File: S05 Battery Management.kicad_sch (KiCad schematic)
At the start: 17 parts, among them Q10 DMT4011LFG, Q11 DMT4011LFG, Q12 DMP3018SFV, Q13 DMP3018SFV, Q14 DMP3018SFV, Q15 DMP3018SFV, Q8 DMT4011LFG, Q9 DMT4011LFG, U1 LTC1960

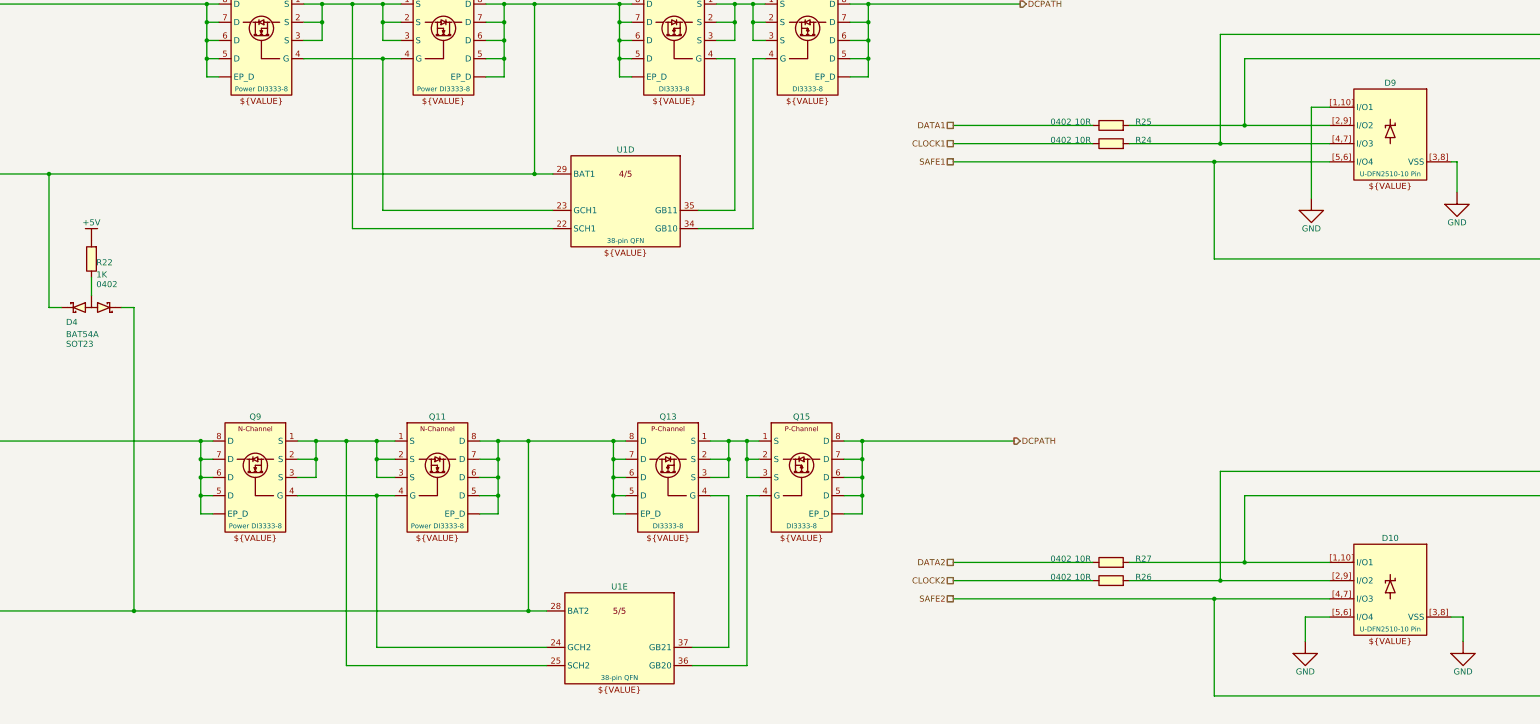
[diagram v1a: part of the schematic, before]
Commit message: Final-revision value changes and standard R/C symbols
Values (schematic and PCB):
- C2 100uF -> 82uF, matching the ordered 35SVPF82M
- C46, C47, C51 (TPS22811 DVDT) 4.7nF -> 1.8nF CC0402KRX7R9BB182 for a
  shorter output ramp
- R24-R27 10R -> 0R; D9, D10 and R36 DNP
- R14 0.01R -> 0.012R PA2512FKF7W0R012E

Symbols:
- All 160 resistors and capacitors now use Device:R, Device:C and
  Device:C_Polarized; the 76 per-value R/C symbols are removed from the
  project library. Connectivity is unchanged (netlist compared).
- Value is now the displayed field instead of ALTIUM_VALUE, which had left
  R1, C39 and R54 showing their old values. ALTIUM_VALUE synced with Value
  on R1, C39, R54, D1, Q1, Q3 and L1.
- Net-(C40-+) is now Net-(U5-ISNSP); renamed on the PCB and in the
  PWR 15A net class pattern.

Co-Authored-By: Claude Opus 5.5 <noreply@anthropic.com>
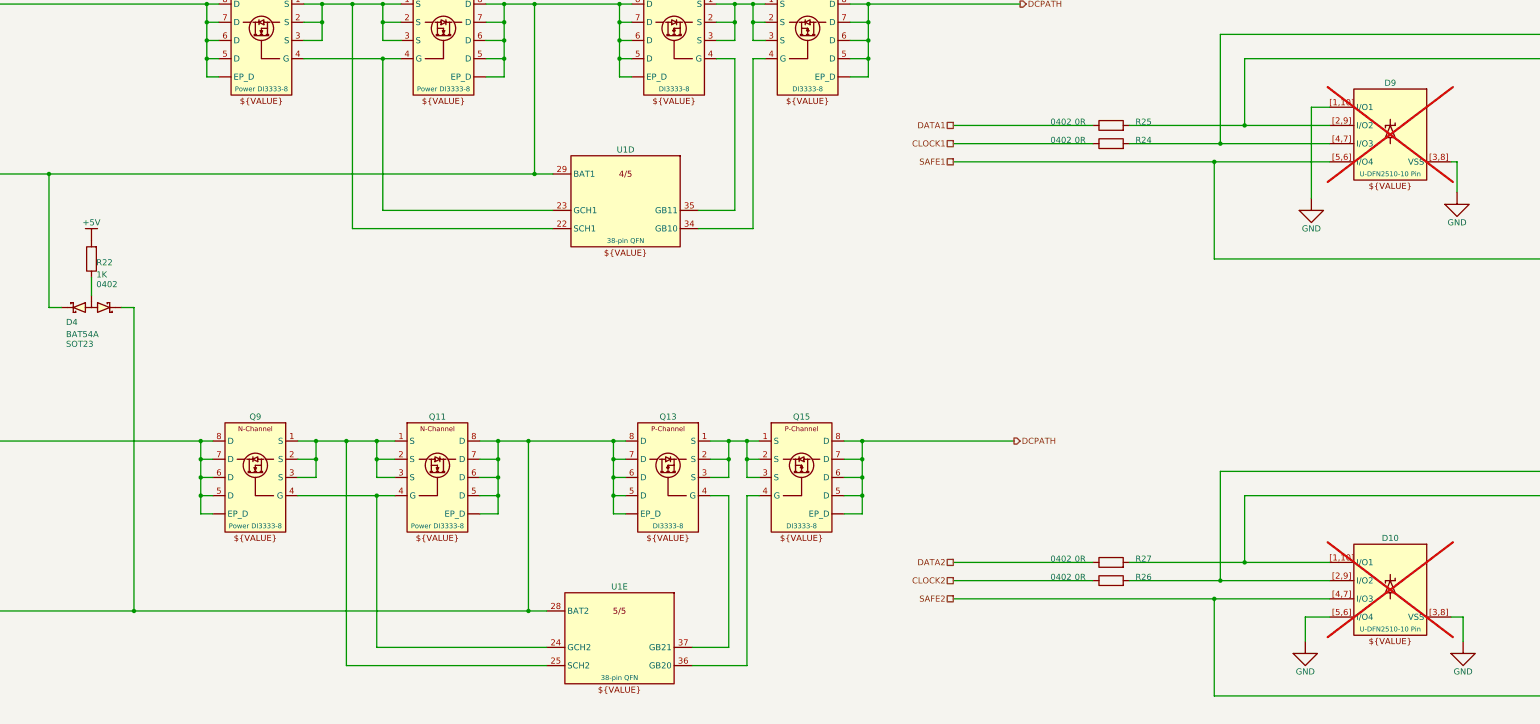
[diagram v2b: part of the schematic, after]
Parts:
- D10, D9: now not fitted
- R22: symbol Lattech Systems:Resistor 1K 1% 0402 -> Device:R
- R24, R25, R26, R27: value 10R -> 0R; symbol Lattech Systems:Resistor 10R 1% 0402 -> Device:R; ALTIUM_VALUE 10R -> 0R

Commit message: Retune load-switch OVLO and PG dividers; add design constraint notes
- R90-R92 1M -> 1.07M: OVLO trips at 14.0 V (13.40-14.69 V) and recovers
  below 12.75 V (at least 12.23 V), so a tripped switch always comes back
  on the 12.03 V rail. R101 (Q23 gate divider) -> 1.07M to share the line.
- PGTH dividers R59/R61/R76 1M -> 100K and R60/R62/R77 130K -> 13K: same
  10.43 V threshold, but the +-1 uA pin leakage now moves it 0.1 V, not
  1 V; worst-case rising 10.93 V instead of 11.84 V.
- Schematic notes for the W16 constraints: J2 contacts (S01), R16 latching
  breaker and ED29/QE29 trip currents (S03), R19 vs L1 saturation (S04),
  R22 presence pull-up (S05), R42 and the U5 MODE/ILIMCOMP/VCC2 pins (S06),
  and the OVLO/PG divider settings (S07).
- README: OVLO and PG divider figures, and the EN_CONST_TDEAD default for
  the I2C build.

Co-Authored-By: Claude Opus 5.5 <noreply@anthropic.com>
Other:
- note added: "R22 = 1K is the D4 battery-presence pull-up: an empty battery slot sits at about 5 V. Expected. Keep R22 at 1K (R54 is 768R; they don't share a value)."
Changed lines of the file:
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@@
 	(generator_version "10.0")
 	(paper "A3")
+	(text "R22 = 1K is the D4 battery-presence pull-up:\nan empty battery slot sits at about 5 V. Expected.\nKeep R22 at 1K (R54 is 768R; they don't share a value)."
+		(exclude_from_sim no)
+		(at 68.58 116.84 0)
+		(effects
+			(font
+				(size 1.27 1.27)
+			)
+			(justify left top)
+		)
+	)
 	(text "MODULE:"
 		(exclude_from_sim no)

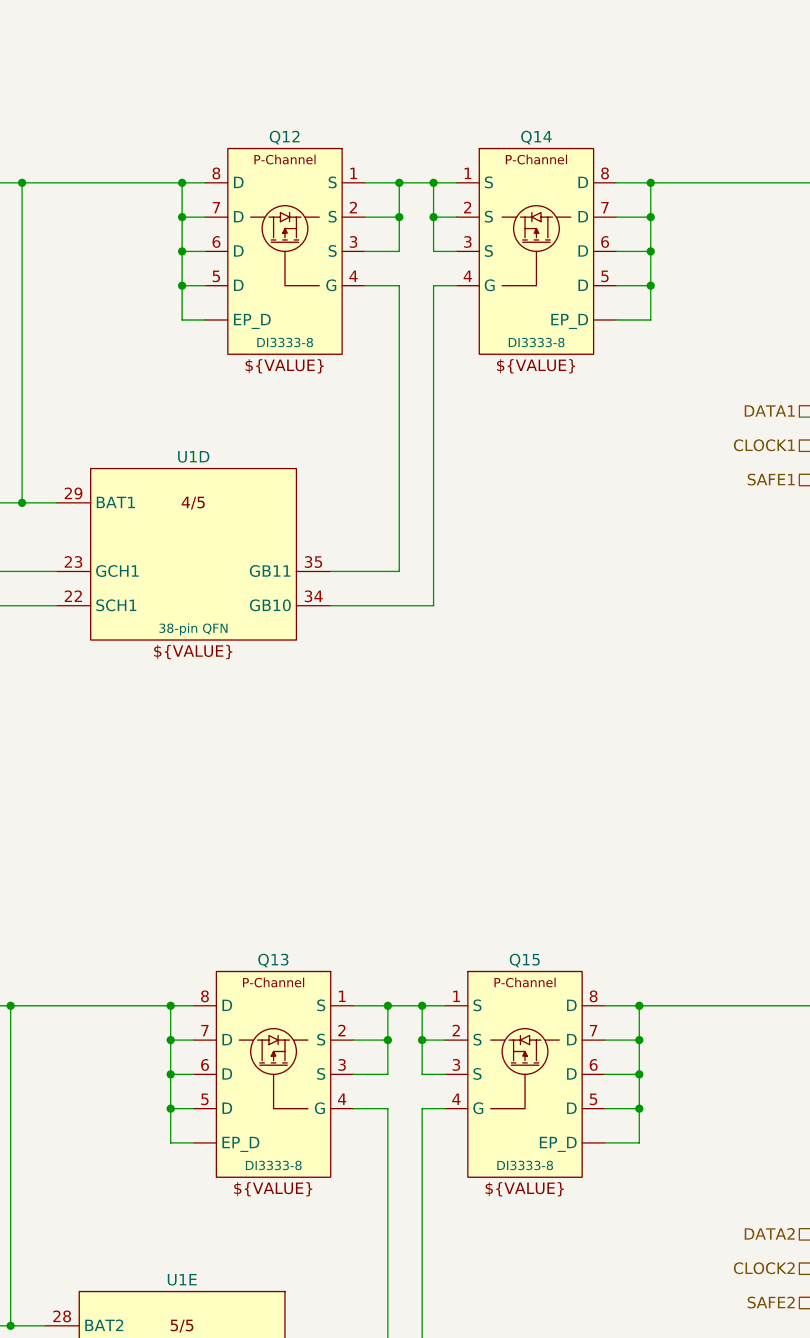
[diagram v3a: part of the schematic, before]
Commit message: Fit DMP3007SCG battery FETs and 1210 snubber resistors
- Q4, Q5, Q12-Q15: DMP3018SFV -> DMP3007SCG-13 (V-DFN3333-8 Type B) on
  KiCad's standard Package_SON:Diodes_PowerDI3333-8, which matches Diodes'
  Type B suggested land apart from 0.1 mm more toe per pad row. The new
  project symbol keeps the old pin positions and numbers D pins 5-8 and
  EP_D all 5, the footprint's single drain pad; all were already one net.
  The unused DMP3018SFV symbol is removed from the project library.
- R41, R45 (SW1/SW2 snubbers): 2.2R 1206 1/4 W -> 2.2R 1% 1210 1/2 W, any
  standard thick film. R41 runs at 75% (0.38 W worst case), R45 at 33%.
- README design-change rows for both.

The PCB still needs Update PCB from Schematic for these and the DAQ UVLO
parts.

Co-Authored-By: Claude Opus 5.5 <noreply@anthropic.com>
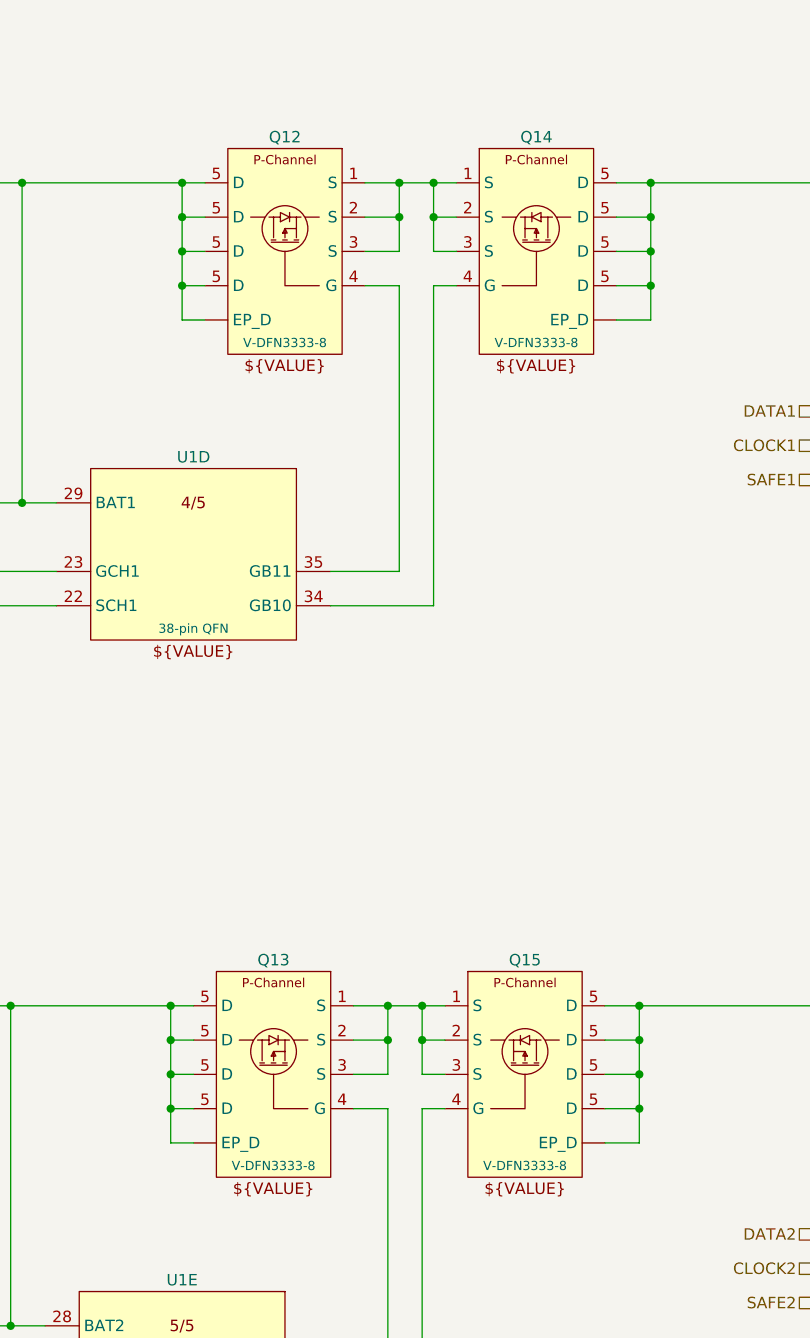
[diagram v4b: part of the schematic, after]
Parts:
- Q12, Q13, Q14, Q15: value DMP3018SFV -> DMP3007SCG-13; footprint EVO2513-0_5_0-import-fps:Power DI3333-8 B3.3 x 3.3 P0.65 Tab 8-Pin -> Package_SON:Diodes_PowerDI3333-8; symbol Lattech Systems:Transistor P-Channel MOSFET 30V DMP3018SFV Power DI3333-8 -> Lattech Systems:Transistor P-Channel MOSFET 30V DMP3007SCG V-DFN3333-8; ALTIUM_FOOTPRINT DI3333-8 -> V-DFN3333-8; ALTIUM_VALUE DMP3018SFV -> DMP3007SCG-13; MANUFACTURER_PN DMP3018SFV -> DMP3007SCG-13
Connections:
- net DCPATH: no longer Q14.6 (D), Q14.7 (D), Q14.8 (D), Q14.9 (EP_D), Q15.6 (D), Q15.7 (D), Q15.8 (D), Q15.9 (EP_D)
- net POS1: no longer Q12.6 (D), Q12.7 (D), Q12.8 (D), Q12.9 (EP_D)
- net POS2: no longer Q13.6 (D), Q13.7 (D), Q13.8 (D), Q13.9 (EP_D)
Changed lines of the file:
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@@
 	)
 	(symbol
-		(lib_id "Lattech Systems:Transistor P-Channel MOSFET  30V DMP3018SFV Power DI3333-8")
+		(lib_id "Lattech Systems:Transistor P-Channel MOSFET 30V DMP3007SCG V-DFN3333-8")
 		(at 181.61 151.13 0)
 		(mirror y)
@@
 			)
 		)
-		(property "Value" "DMP3018SFV"
+		(property "Value" "DMP3007SCG-13"
 			(at 168.91 149.86 0)
 			(hide yes)
@@
 			)
 		)
-		(property "Footprint" "EVO2513-0_5_0-import-fps:Power DI3333-8 B3.3 x 3.3 P0.65 Tab 8-Pin"
+		(property "Footprint" "Package_SON:Diodes_PowerDI3333-8"
 			(at 181.61 151.13 0)
 			(hide yes)
@@
 			)
 		)
-		(property "Description" "Transistor P-Channel MOSFET  30V DMP3018SFV Power DI3333-8"
+		(property "Description" "Transistor P-Channel MOSFET 30V DMP3007SCG-13 V-DFN3333-8 (Type B)"
 			(at 181.61 151.13 0)
 			(hide yes)
@@
 			)
 		)
-		(property "ALTIUM_FOOTPRINT" "DI3333-8"
+		(property "ALTIUM_FOOTPRINT" "V-DFN3333-8"
 			(at 172.72 168.9098 0)
 			(show_name no)
@@
 			)
 		)
-		(property "ALTIUM_VALUE" "DMP3018SFV"
+		(property "ALTIUM_VALUE" "DMP3007SCG-13"
 			(at 191.262 148.336 0)
 			(hide yes)
@@
 			)
 		)
-		(property "MANUFACTURER_PN" "DMP3018SFV"
+		(property "MANUFACTURER_PN" "DMP3007SCG-13"
 			(at 181.102 144.78 0)
 			(hide yes)
@@
 		(pin "5"
 		)
-		(pin "7"
-		)
 		(pin "4"
 		)
 		(pin "2"
 		)
-		(pin "6"
-		)
-		(pin "8"
-		)
-		(pin "9"
-		)
 		(instances
 			(project "EVO2513-0_5_0"
@@
 	)
 	(symbol
-		(lib_id "Lattech Systems:Transistor P-Channel MOSFET  30V DMP3018SFV Power DI3333-8")
+		(lib_id "Lattech Systems:Transistor P-Channel MOSFET 30V DMP3007SCG V-DFN3333-8")
 		(at 193.04 59.69 0)
 		(unit 1)
@@
 			)
 		)
-		(property "Value" "DMP3018SFV"
+		(property "Value" "DMP3007SCG-13"
 			(at 205.74 58.42 0)
 			(hide yes)
@@
 			)
 		)
-		(property "Footprint" "EVO2513-0_5_0-import-fps:Power DI3333-8 B3.3 x 3.3 P0.65 Tab 8-Pin"
+		(property "Footprint" "Package_SON:Diodes_PowerDI3333-8"
 			(at 193.04 59.69 0)
 			(hide yes)
@@
 			)
 		)
-		(property "Description" "Transistor P-Channel MOSFET  30V DMP3018SFV Power DI3333-8"
+		(property "Description" "Transistor P-Channel MOSFET 30V DMP3007SCG-13 V-DFN3333-8 (Type B)"
 			(at 193.04 59.69 0)
 			(hide yes)
@@
 			)
 		)
-		(property "ALTIUM_FOOTPRINT" "DI3333-8"
+		(property "ALTIUM_FOOTPRINT" "V-DFN3333-8"
 			(at 201.93 77.4698 0)
 			(show_name no)
@@
 			)
 		)
-		(property "ALTIUM_VALUE" "DMP3018SFV"
+		(property "ALTIUM_VALUE" "DMP3007SCG-13"
 			(at 183.388 56.896 0)
 			(hide yes)
@@
 			)
 		)
-		(property "MANUFACTURER_PN" "DMP3018SFV"
+		(property "MANUFACTURER_PN" "DMP3007SCG-13"
 			(at 192.532 53.34 0)
 			(hide yes)
@@
 		(pin "5"
 		)
-		(pin "7"
-		)
 		(pin "4"
 		)
 		(pin "2"
 		)
-		(pin "6"
-		)
-		(pin "8"
-		)
-		(pin "9"
-		)
 		(instances
 			(project "EVO2513-0_5_0"
@@
 	)
 	(symbol
-		(lib_id "Lattech Systems:Transistor P-Channel MOSFET  30V DMP3018SFV Power DI3333-8")
+		(lib_id "Lattech Systems:Transistor P-Channel MOSFET 30V DMP3007SCG V-DFN3333-8")
 		(at 182.88 59.69 0)
 		(mirror y)
@@
 			)
 		)
-		(property "Value" "DMP3018SFV"
+		(property "Value" "DMP3007SCG-13"
 			(at 170.18 58.42 0)
 			(hide yes)
@@
 			)
 		)
-		(property "Footprint" "EVO2513-0_5_0-import-fps:Power DI3333-8 B3.3 x 3.3 P0.65 Tab 8-Pin"
+		(property "Footprint" "Package_SON:Diodes_PowerDI3333-8"
 			(at 182.88 59.69 0)
 			(hide yes)
@@
 			)
 		)
-		(property "Description" "Transistor P-Channel MOSFET  30V DMP3018SFV Power DI3333-8"
+		(property "Description" "Transistor P-Channel MOSFET 30V DMP3007SCG-13 V-DFN3333-8 (Type B)"
 			(at 182.88 59.69 0)
 			(hide yes)
@@
 			)
 		)
-		(property "ALTIUM_FOOTPRINT" "DI3333-8"
+		(property "ALTIUM_FOOTPRINT" "V-DFN3333-8"
 			(at 173.99 77.4698 0)
 			(show_name no)
@@
 			)
 		)
-		(property "ALTIUM_VALUE" "DMP3018SFV"
+		(property "ALTIUM_VALUE" "DMP3007SCG-13"
 			(at 192.532 56.896 0)
 			(hide yes)
@@
 			)
 		)
-		(property "MANUFACTURER_PN" "DMP3018SFV"
+		(property "MANUFACTURER_PN" "DMP3007SCG-13"
 			(at 182.372 53.34 0)
 			(hide yes)
@@
 		(pin "5"
 		)
-		(pin "7"
-		)
 		(pin "4"
 		)
 		(pin "2"
 		)
-		(pin "6"
-		)
-		(pin "8"
-		)
-		(pin "9"
-		)
 		(instances
 			(project "EVO2513-0_5_0"
@@
 	)
 	(symbol
-		(lib_id "Lattech Systems:Transistor P-Channel MOSFET  30V DMP3018SFV Power DI3333-8")
+		(lib_id "Lattech Systems:Transistor P-Channel MOSFET 30V DMP3007SCG V-DFN3333-8")
 		(at 191.77 151.13 0)
 		(unit 1)
@@
 			)
 		)
-		(property "Value" "DMP3018SFV"
+		(property "Value" "DMP3007SCG-13"
 			(at 204.47 149.86 0)
 			(hide yes)
@@
 			)
 		)
-		(property "Footprint" "EVO2513-0_5_0-import-fps:Power DI3333-8 B3.3 x 3.3 P0.65 Tab 8-Pin"
+		(property "Footprint" "Package_SON:Diodes_PowerDI3333-8"
 			(at 191.77 151.13 0)
 			(hide yes)
@@
 			)
 		)
-		(property "Description" "Transistor P-Channel MOSFET  30V DMP3018SFV Power DI3333-8"
+		(property "Description" "Transistor P-Channel MOSFET 30V DMP3007SCG-13 V-DFN3333-8 (Type B)"
 			(at 191.77 151.13 0)
 			(hide yes)
@@
 			)
 		)
-		(property "ALTIUM_FOOTPRINT" "DI3333-8"
+		(property "ALTIUM_FOOTPRINT" "V-DFN3333-8"
 			(at 200.66 168.9098 0)
 			(show_name no)
@@
 			)
 		)
-		(property "ALTIUM_VALUE" "DMP3018SFV"
+		(property "ALTIUM_VALUE" "DMP3007SCG-13"
 			(at 182.118 148.336 0)
 			(hide yes)
@@
 			)
 		)
-		(property "MANUFACTURER_PN" "DMP3018SFV"
+		(property "MANUFACTURER_PN" "DMP3007SCG-13"
 			(at 191.262 144.78 0)
 			(hide yes)
@@
 			)
 		)
-		(pin "6"
-		)
 		(pin "3"
 		)
@@
 		(pin "5"
 		)
-		(pin "7"
-		)
 		(pin "4"
 		)
 		(pin "2"
 		)
-		(pin "8"
-		)
-		(pin "9"
-		)
 		(instances
